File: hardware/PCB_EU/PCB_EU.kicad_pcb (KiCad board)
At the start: 4 copper layers, 100 x 100 mm, 200 parts, among them J101 24 V IN, J201 UART 3V3, J301 MEM2061 SPI, J401 SHT4x XH2.54-4P-90, J403 FLOAT / GND, J411 FAN1 2510-4P, J421 FAN2 2510-4P, J501 LED1 + / GND, J601 LED2 + / GND, J602 BAR2 + / GND, J701 PTC + / RETURN, J702 PUMP + / RETURN, Q102 IRF1010ESPBF, Q411 FAN1 AO3422, Q421 FAN2 AO3422, Q501 TK22E10N1, Q601 TK22E10N1, Q701 BC847B-DIO, Q702 BC857B, Q703 IRF1010ESPBF, Q704 AO3422, SW201 RESET, SW202 BOOT, U101 L7987 3A, U102 INA226, U201 AP63203WU-7, U202 ESP32-WROOM-32E-N4, U301 MCP7940N-I/SN, U401 USBLC6-2SC6, U402 USBLC6-2SC6, U501 LM3429MH/NOPB, U601 LM3429MH/NOPB, U802 LM2903D-ST, Y301 32.768k CL7p

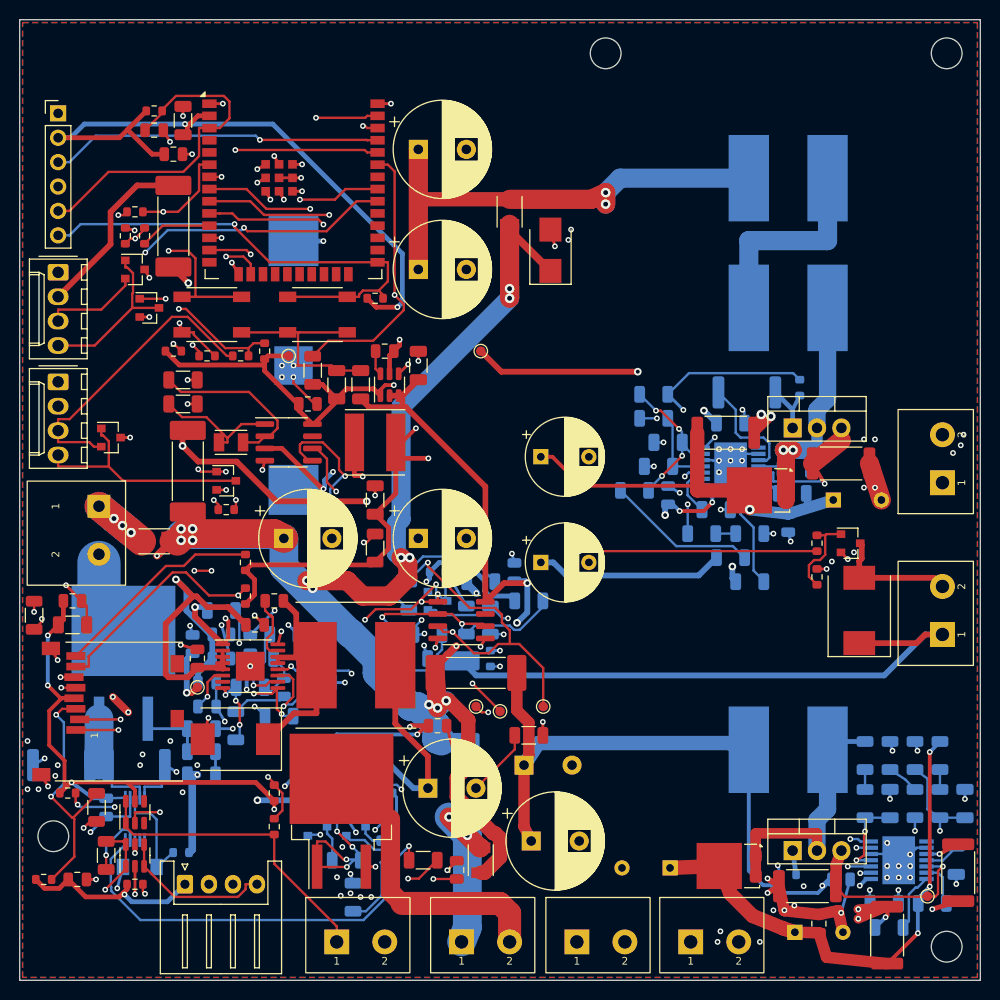
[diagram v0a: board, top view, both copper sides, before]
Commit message: PCB_EU: all electrolytic capacitors on the top side
Per Igors (22.10.2026): move every electrolytic to one side so the assembled
board is thinner.

- C508, C601, C608, C609 move from the bottom to the top, into the column
  x 61-74 mm between C510/C602 and L601 that the removed HS2 reserve freed.
  All twelve electrolytics are now on the top; the tallest bottom part is the
  8.05 mm JNRH1207 inductor (was the 16.15 mm C601): stack 37.9 -> 29.8 mm.
- LED2 output bank: D601 -> C608 -> C609 on F.Cu 1.5 mm, D601 -> C611 direct;
  LED2 input: F104.2 -> C601 on F.Cu 1.2 mm, C601 -> L601 on B.Cu 1.5 mm
  (10 mm instead of 25); LED1: the R501 -> C508 GND link and the C511 -> C508
  bypass are dropped, C508 is autorouted like C509/C510.
- PCB_EU.kicad_dru has no rules any more: the solid GND connections of C609 and
  C510 are not needed, DRC is clean without them.
- New Freerouting run; routing/pass1.ses and pass2.ses replaced.

Checks (KiCad 10.0.7): ERC 0, 56 connectivity checks, 22639 placement checks,
DRC 0 / parity 0 / unconnected 0, 1425 tracks / 327 vias, rebuild from the
repository byte-identical (two runs). ampacity.py unchanged: worst IPC-2221
rise 38 C. Open for the prototype: capacitor temperatures next to D601 and
L601, LED1/LED2 ripple, LED_NDIM escape 0.22 mm from LED2_SW.

Co-Authored-By: Claude Sonnet 5.5 <noreply@anthropic.com>
Claude-Session: https://claude.ai/code/session_01AxccZX6Cb4FnRKJMrFYMSX
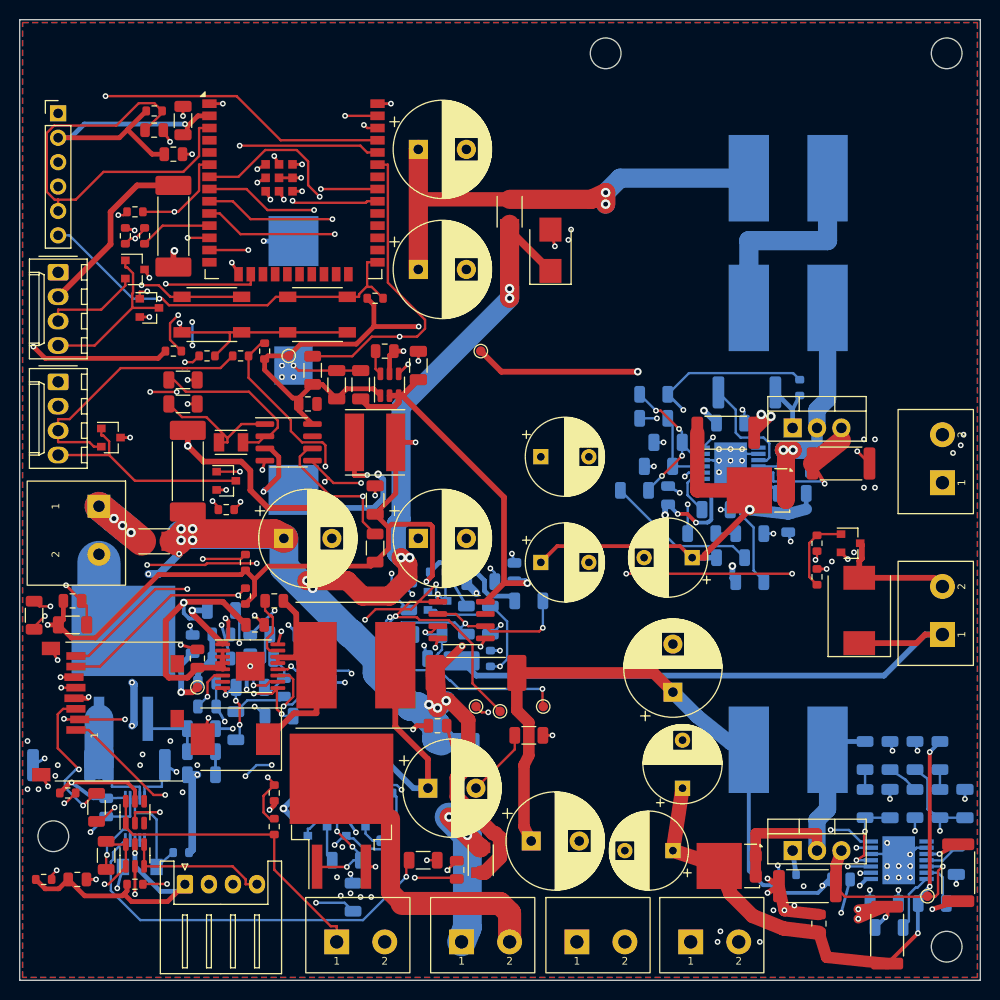
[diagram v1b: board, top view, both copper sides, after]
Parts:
- C508, C601, C608, C609: moved to F.Cu
- moved C609 19.0 mm to (69.0, 80.0), turned to 90 degrees
- moved C601 17.3 mm to (68.0, 70.0), turned to 90 degrees
- moved C508 15.9 mm to (70.0, 56.0), turned to 180 degrees
- moved C608 1.82 mm to (68.0, 86.5)
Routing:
- net FAN2_TACH: track 28.7 -> 62.7 mm
- net +3V3: track 326.5 -> 345.8 mm, vias 15 -> 11
- net BLOCK_OC: track 48.2 -> 63.5 mm, vias 9 -> 7
- net LED1_OUT: track 72.4 -> 59.8 mm
- net UVLO_SENSE: track 43.4 -> 31.3 mm, vias 2 -> 3
- net GND: track 208.0 -> 198.3 mm, vias 137 -> 138
- net ESP_EN: track 62.7 -> 72.1 mm
- net I2C_SDA: track 127.8 -> 118.8 mm, vias 4 -> 6
- net ESP_BOOT: track 50.9 -> 41.9 mm
- net I2C_SCL: track 135.5 -> 144.5 mm, vias 4 -> 3
- net FAN2_GATE: track 22.0 -> 30.2 mm, vias 4 -> 3
- net PTC_GATE: track 21.0 -> 13.0 mm, vias 4 -> 3
- net LED2_OUT: track 53.3 -> 59.8 mm
- net +24V_AUX: track 85.0 -> 89.8 mm, vias 3 -> 4
- net UART_TX: track 34.6 -> 39.3 mm
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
